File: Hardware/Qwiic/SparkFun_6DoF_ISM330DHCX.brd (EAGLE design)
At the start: 25.4 x 25.4 mm, 70 parts, among them J1 QWIIC_RIGHT_ANGLE, J2 QWIIC_RIGHT_ANGLE, U1 ISM330DHCX

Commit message: Fixes swapped silk on PICO and CS headers, changes to v10, adds "default" text to default address
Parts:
- moved U$18 2.54 mm to (19.1, 4.22)
- moved U$27 2.54 mm to (16.5, 3.35)
- moved U$3 2.54 mm to (16.5, 3.35)
- moved U$6 2.54 mm to (19.1, 4.22)
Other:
- board text added: "v10"
- board text removed: "v01"
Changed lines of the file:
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@@
 <setting verticaltext="up"/>
 </settings>
-<grid distance="0.05" unitdist="inch" unit="inch" style="dots" multiple="1" display="yes" altdistance="0.001" altunitdist="inch" altunit="inch"/>
+<grid distance="0.05" unitdist="inch" unit="inch" style="dots" multiple="1" display="yes" altdistance="0.005" altunitdist="inch" altunit="inch"/>
 <layers>
 <layer number="1" name="Top" color="4" fill="1" visible="yes" active="yes"/>
@@
 <wire x1="0" y1="0" x2="25.4" y2="0" width="0.2032" layer="20"/>
 <wire x1="25.4" y1="0" x2="25.4" y2="25.4" width="0.2032" layer="20"/>
-<text x="24.139525" y="11.420475" size="0.8128" layer="16" font="vector" ratio="22" rot="MR90">v01</text>
+<text x="24.139525" y="11.420475" size="0.8128" layer="16" font="vector" ratio="22" rot="MR90">v10</text>
 <wire x1="0.3302" y1="7.546975" x2="2.2352" y2="7.546975" width="0.254" layer="21"/>
 <wire x1="1.7272" y1="7.038975" x2="1.7272" y2="8.181975" width="0.254" layer="21" curve="-180"/>
@@
 <attribute name="VALUE" x="22.86" y="21.209" size="0.6096" layer="27" font="vector" ratio="20" align="top-center"/>
 </element>
-<element name="U$3" library="top" package="##CS##7" value="" x="19.0754" y="3.3528" smashed="yes" rot="R90"/>
-<element name="U$27" library="bot" package="##CS##8" value="" x="19.0754" y="3.3528" smashed="yes" rot="MR270"/>
+<element name="U$3" library="top" package="##CS##7" value="" x="16.5354" y="3.3528" smashed="yes" rot="R90"/>
+<element name="U$27" library="bot" package="##CS##8" value="" x="16.5354" y="3.3528" smashed="yes" rot="MR270"/>
 <element name="U$31" library="top" package="6DOF12" value="" x="5.6896" y="12.8524" smashed="yes" rot="MR270"/>
 <element name="R5" library="SparkFun-Resistors" package="0603" value="10k" x="17.272" y="14.3764" smashed="yes" rot="R90">
@@
 <element name="U$33" library="ISMTop" package="#POCIX#7" value="" x="19.05" y="20.7772" smashed="yes" rot="MR270"/>
 <element name="U$26" library="ISMTop" package="#PICO#13" value="" x="11.43" y="4.1656" smashed="yes" rot="MR270"/>
-<element name="U$6" library="ISMTop" package="#POCI#11" value="" x="16.51" y="4.2164" smashed="yes" rot="MR270"/>
-<element name="U$18" library="ISMTop" package="#POCI#12" value="" x="16.51" y="4.2164" smashed="yes" rot="R90"/>
+<element name="U$6" library="ISMTop" package="#POCI#11" value="" x="19.05" y="4.2164" smashed="yes" rot="MR270"/>
+<element name="U$18" library="ISMTop" package="#POCI#12" value="" x="19.05" y="4.2164" smashed="yes" rot="R90"/>
 <element name="U$34" library="ISMTopMini" package="X2114" value="" x="1.651" y="6.35" smashed="yes"/>
 <element name="U$35" library="ISMTopMini" package="Y2115" value="" x="4.826" y="5.461" smashed="yes"/>

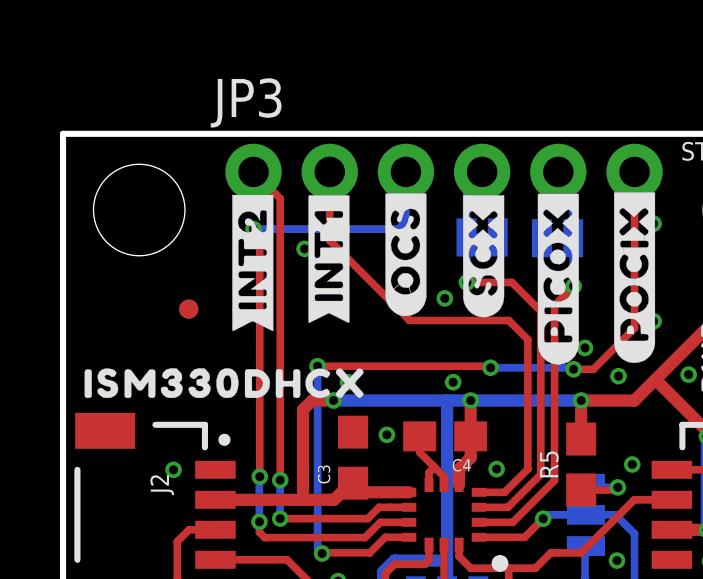
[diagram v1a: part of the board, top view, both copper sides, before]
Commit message: Updates INT2 to rounded, and changes INT text on Micro to INT1
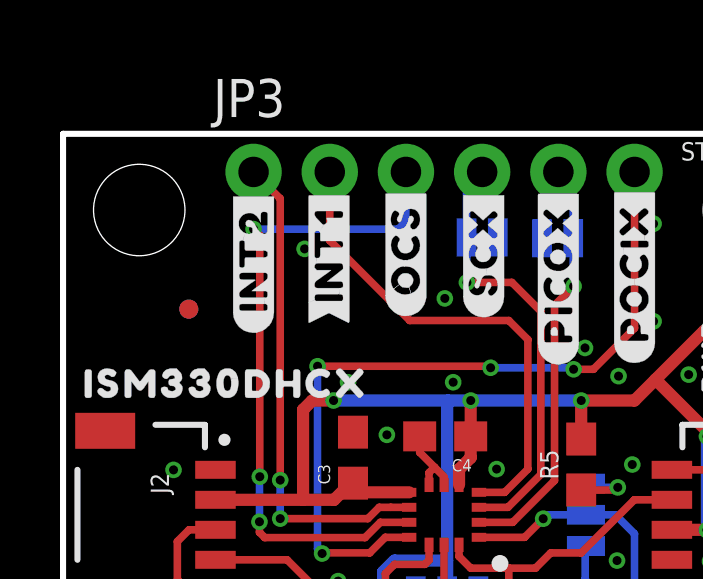
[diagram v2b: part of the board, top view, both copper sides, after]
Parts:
- removed U$21: (no value), bot:#INT2#9
- added U$40: (no value), top:#INT2#3
- U$8: device top:#INT2#9 -> top:#INT2#2
- moved U$8 0.06 mm to (6.35, 21.2), flipped to the bottom, turned to 270 degrees
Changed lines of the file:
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@@
 <element name="U$28" library="top" package="PWR8" value="" x="21.6408" y="18.034" smashed="yes" rot="R90"/>
 <element name="U$7" library="top" package="#INT1#9" value="" x="8.8646" y="21.3868" smashed="yes" rot="R90"/>
-<element name="U$8" library="top" package="#INT2#9" value="" x="6.3246" y="21.2598" smashed="yes" rot="R90"/>
 <element name="U$19" library="bot" package="#INT1#9" value="" x="8.8646" y="21.3868" smashed="yes" rot="MR270"/>
-<element name="U$21" library="bot" package="#INT2#9" value="" x="6.3246" y="21.2598" smashed="yes" rot="MR270"/>
 <element name="STANDOFF4" library="SparkFun-Hardware" package="STAND-OFF-TIGHT" value="STAND-OFFTIGHT" x="22.86" y="22.86" smashed="yes">
 <attribute name="NAME" x="22.86" y="24.511" size="0.6096" layer="25" font="vector" ratio="20" align="bottom-center"/>
@@
 <element name="U$38" library="ISMTopMini" package="Y2115" value="" x="24.13" y="6.985" smashed="yes" rot="MR0"/>
 <element name="U$39" library="ISMTopMini" package="Z2116" value="" x="24.511" y="9.017" smashed="yes" rot="MR0"/>
+<element name="U$40" library="top" package="#INT2#3" value="" x="6.35" y="21.209" smashed="yes" rot="R90"/>
+<element name="U$8" library="top" package="#INT2#2" value="" x="6.35" y="21.209" smashed="yes" rot="MR270"/>
 </elements>
 <signals>

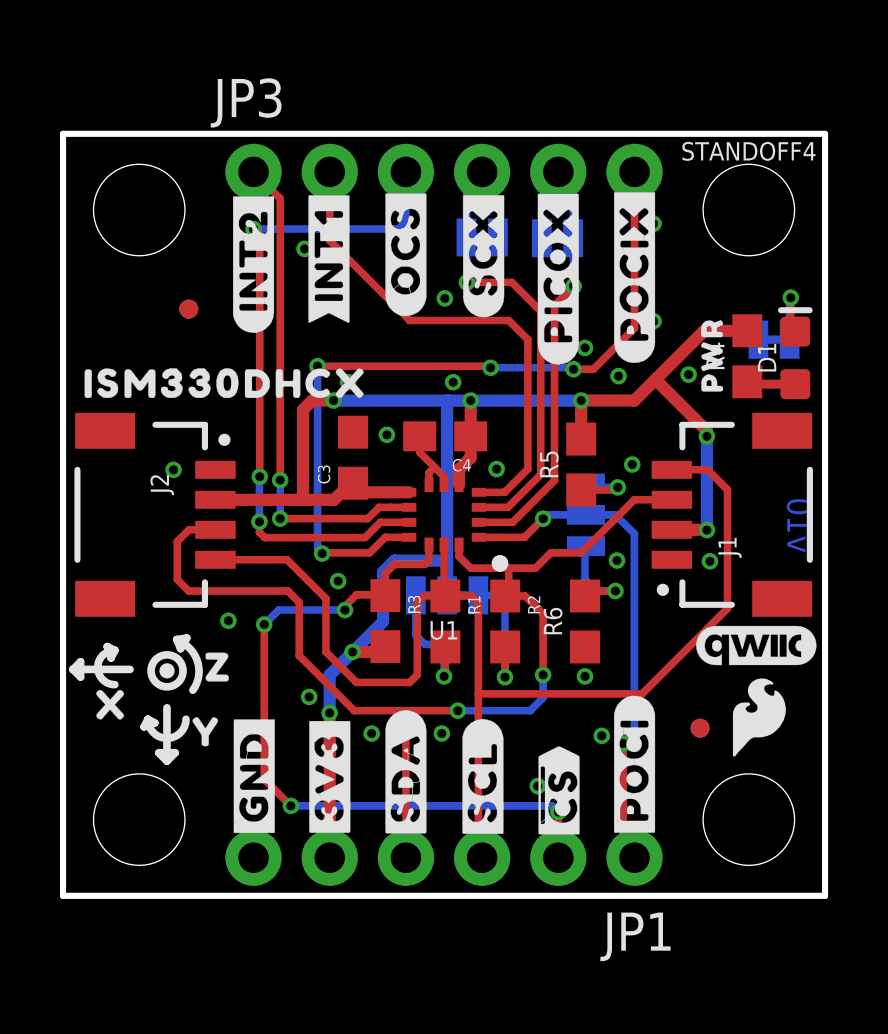
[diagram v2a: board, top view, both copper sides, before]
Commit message: Adds a via, adds some clearer text to the schematic
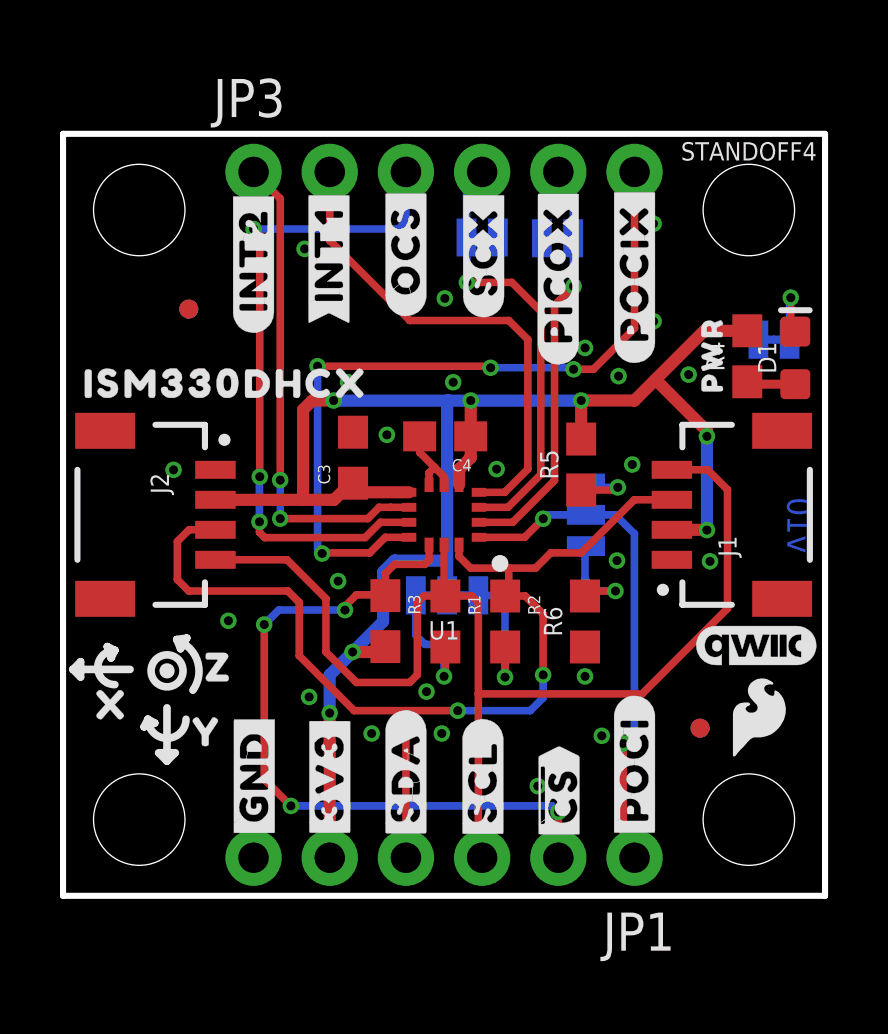
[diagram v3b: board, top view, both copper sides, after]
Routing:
- net GND: vias 23 -> 24
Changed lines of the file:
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@@
 <wire x1="11.8881" y1="14.7819" x2="11.8881" y2="15.3162" width="0.254" layer="1"/>
 <via x="8.0518" y="21.5646" extent="1-16" drill="0.3"/>
+<via x="12.1158" y="6.8072" extent="1-16" drill="0.3"/>
 </signal>
 <signal name="SCL">
